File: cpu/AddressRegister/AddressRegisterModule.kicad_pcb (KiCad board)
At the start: 2 copper layers, 100 x 80 mm, 53 parts, among them J1 Bus_PCI_32bit_5V, U1 74LS193, U10 74LS245, U11 74LS245, U12 74LS00, U2 74LS193, U3 74LS193, U4 74LS193, U5 74LS245, U6 74LS245, U7 74LS245, U8 74LS245, U9 74LS245

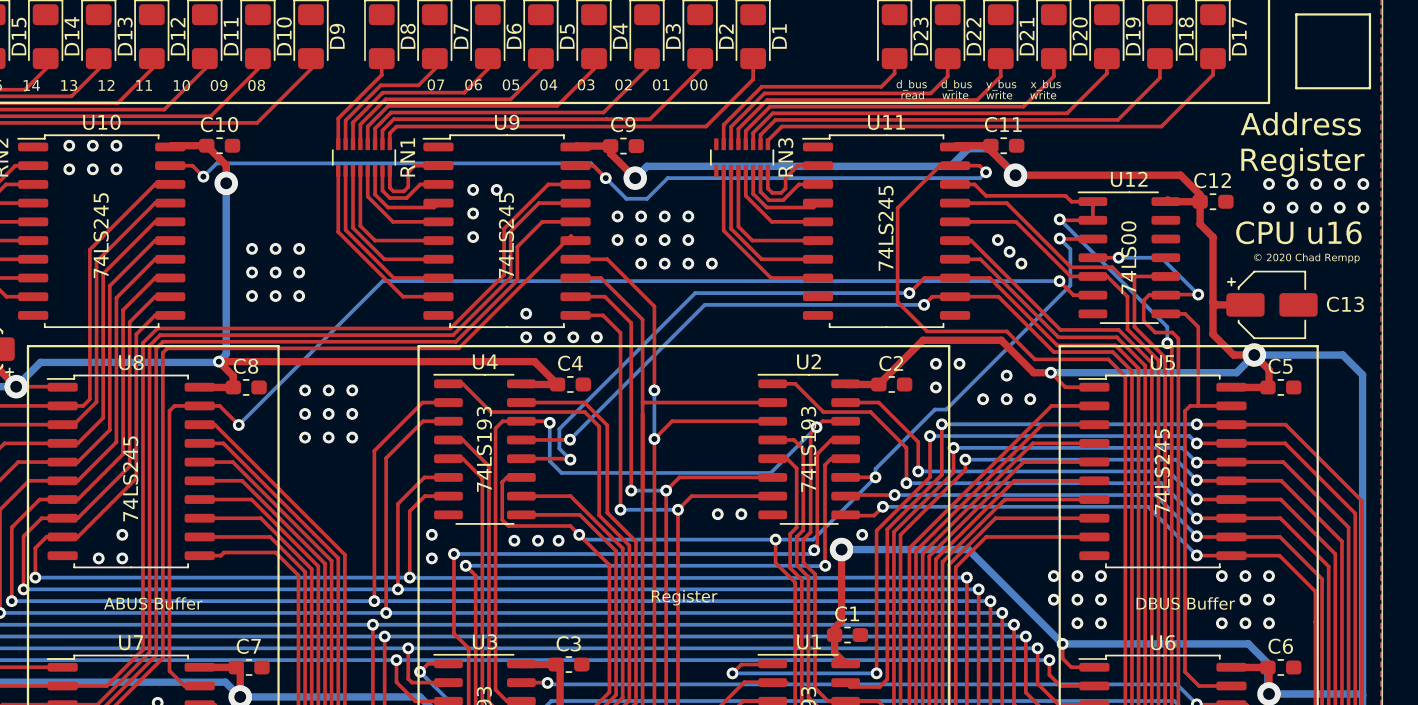
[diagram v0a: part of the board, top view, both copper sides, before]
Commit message: Finishing touches on GPR and Address Register
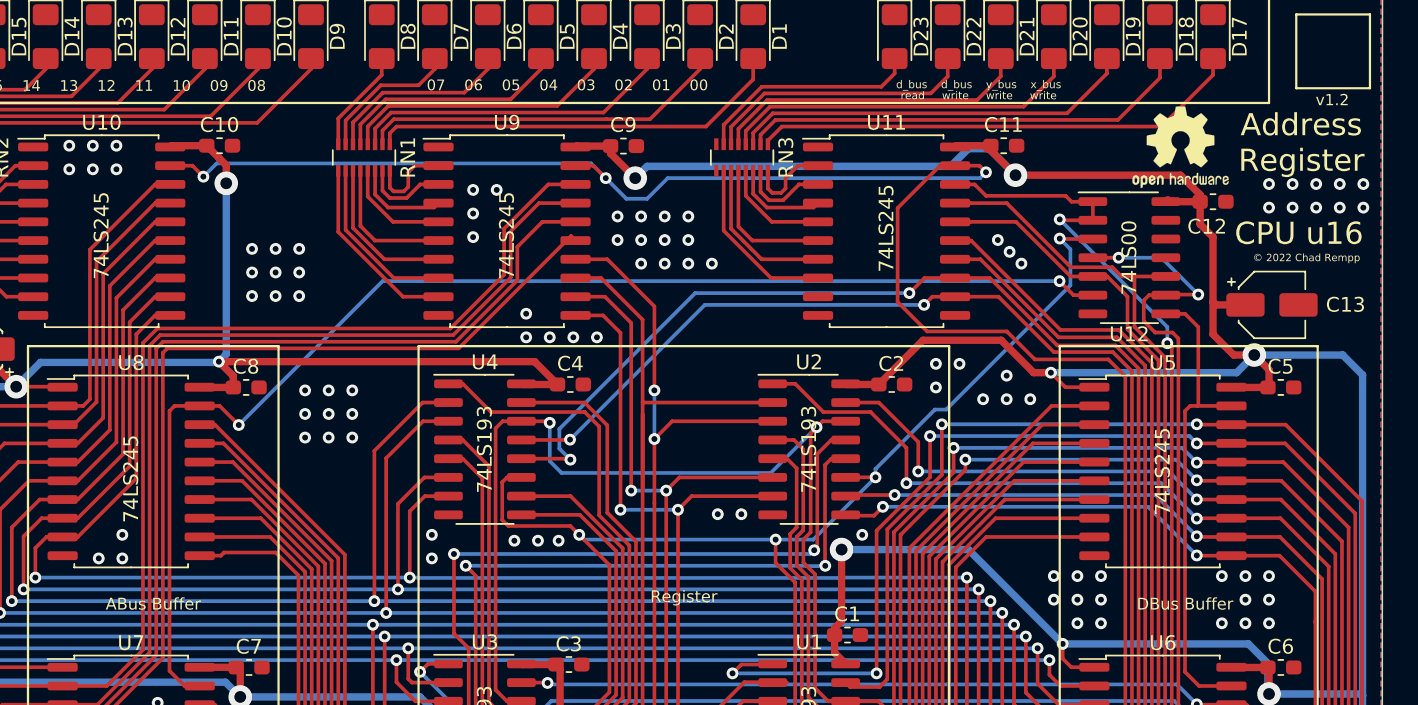
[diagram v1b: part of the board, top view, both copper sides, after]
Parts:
- added REF**: OSHW-Logo2_7.3x6mm_SilkScreen, Symbol:OSHW-Logo2_7.3x6mm_SilkScreen, F.Cu at (203.2, 51.5)
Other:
- board text added: "ABus Buffer"
- board text added: "DBus Buffer"
- board text added: "v1.2"
- board text added: "© 2022 Chad Rempp"
- board text removed: "ABUS Buffer"
- board text removed: "DBUS Buffer"
- board text removed: "© 2020 Chad Rempp"

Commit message: Upgrade to KiCad 6 and commit a bunch of random stuff
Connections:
- net /~CLK renamed /~{CLK}
- net /~DBG renamed /~{DBG}
- net /~a_bus_write_CLK renamed /~{a_bus_write_CLK}
- net /~d_bus_read renamed /~{d_bus_read}
- net /~d_bus_write_CLK renamed /~{d_bus_write_CLK}
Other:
- net class Default removed
- net class Power removed

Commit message: Address Register v1.3
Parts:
- added R1: 1K, Resistor_SMD:R_0603_1608Metric_Pad0.98x0.95mm_HandSolder, F.Cu at (150.5, 114.2)
- added R2: 1K, Resistor_SMD:R_0603_1608Metric_Pad0.98x0.95mm_HandSolder, F.Cu at (150.5, 112.6)
- added R3: 1K, Resistor_SMD:R_0603_1608Metric_Pad0.98x0.95mm_HandSolder, F.Cu at (150.5, 94.7)
- added R4: 1K, Resistor_SMD:R_0603_1608Metric_Pad0.98x0.95mm_HandSolder, F.Cu at (150.5, 96.3)
- added R5: 1K, Resistor_SMD:R_0603_1608Metric_Pad0.98x0.95mm_HandSolder, F.Cu at (128.5, 114.2)
- added R6: 1K, Resistor_SMD:R_0603_1608Metric_Pad0.98x0.95mm_HandSolder, F.Cu at (128.5, 112.6)
- added R7: 1K, Resistor_SMD:R_0603_1608Metric_Pad0.98x0.95mm_HandSolder, F.Cu at (128.5, 94.7)
- added R8: 1K, Resistor_SMD:R_0603_1608Metric_Pad0.98x0.95mm_HandSolder, F.Cu at (128.5, 96.3)
- C1, C10, C11, C12, C2, C3, C4, C5, C6, C7, C8, C9: value e -> 0.1uF
- moved D17 53.3 mm to (154.4, 59.4)
- moved D18 52.2 mm to (151.9, 59.4)
- moved D19 51.2 mm to (149.4, 59.4)
- moved D20 50.2 mm to (146.8, 59.4)
- moved D21 49.2 mm to (144.3, 59.4)
- moved D22 48.2 mm to (141.7, 59.4)
- moved D23 47.2 mm to (139.2, 59.4)
- moved D1 43.4 mm to (133.6, 59.4)
- moved C8 43.4 mm to (110.4, 99.7), turned to 0 degrees
- moved U8 42.5 mm to (106.7, 107.7)
- moved D2 42.4 mm to (131.1, 59.4)
- moved D3 41.5 mm to (128.5, 59.4)
- moved D4 40.5 mm to (126.0, 59.4)
- moved D5 39.5 mm to (123.4, 59.4)
- moved D6 38.5 mm to (120.9, 59.4)
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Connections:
- J1 pad A1: Net-(J1-PadA1) -> unconnected-(J1-PadA1)
- J1 pad A10: Net-(J1-PadA10) -> unconnected-(J1-PadA10)
- J1 pad A11: Net-(J1-PadA11) -> unconnected-(J1-PadA11)
- J1 pad A12: Net-(J1-PadA12) -> unconnected-(J1-PadA12)
- J1 pad A13: Net-(J1-PadA13) -> unconnected-(J1-PadA13)
- J1 pad A14: Net-(J1-PadA14) -> unconnected-(J1-PadA14)
- J1 pad A15: Net-(J1-PadA15) -> unconnected-(J1-PadA15)
- J1 pad A16: Net-(J1-PadA16) -> unconnected-(J1-PadA16)
- J1 pad A17: Net-(J1-PadA17) -> unconnected-(J1-PadA17)
- J1 pad A18: Net-(J1-PadA18) -> unconnected-(J1-PadA18)
- J1 pad A19: Net-(J1-PadA19) -> unconnected-(J1-PadA19)
- J1 pad A2: Net-(J1-PadA2) -> unconnected-(J1-PadA2)
- J1 pad A20: Net-(J1-PadA20) -> unconnected-(J1-PadA20)
- J1 pad A21: Net-(J1-PadA21) -> unconnected-(J1-PadA21)
- J1 pad A22: Net-(J1-PadA22) -> unconnected-(J1-PadA22)
- J1 pad A23: Net-(J1-PadA23) -> unconnected-(J1-PadA23)
- J1 pad A24: Net-(J1-PadA24) -> unconnected-(J1-PadA24)
- J1 pad A25: Net-(J1-PadA25) -> unconnected-(J1-PadA25)
- J1 pad A26: Net-(J1-PadA26) -> unconnected-(J1-PadA26)
- J1 pad A27: Net-(J1-PadA27) -> unconnected-(J1-PadA27)
- J1 pad A28: Net-(J1-PadA28) -> unconnected-(J1-PadA28)
- J1 pad A29: Net-(J1-PadA29) -> unconnected-(J1-PadA29)
- J1 pad A3: Net-(J1-PadA3) -> unconnected-(J1-PadA3)
- J1 pad A30: Net-(J1-PadA30) -> unconnected-(J1-PadA30)
- J1 pad A31: Net-(J1-PadA31) -> unconnected-(J1-PadA31)
- J1 pad A32: Net-(J1-PadA32) -> unconnected-(J1-PadA32)
- J1 pad A33: Net-(J1-PadA33) -> unconnected-(J1-PadA33)
- J1 pad A34: Net-(J1-PadA34) -> unconnected-(J1-PadA34)
- J1 pad A35: Net-(J1-PadA35) -> unconnected-(J1-PadA35)
- J1 pad A36: Net-(J1-PadA36) -> unconnected-(J1-PadA36)
- J1 pad A37: Net-(J1-PadA37) -> unconnected-(J1-PadA37)
- J1 pad A38: Net-(J1-PadA38) -> unconnected-(J1-PadA38)
- J1 pad A39: Net-(J1-PadA39) -> unconnected-(J1-PadA39)
- J1 pad A4: Net-(J1-PadA4) -> unconnected-(J1-PadA4)
- J1 pad A40: Net-(J1-PadA40) -> unconnected-(J1-PadA40)
- J1 pad A41: Net-(J1-PadA41) -> unconnected-(J1-PadA41)
- J1 pad A42: Net-(J1-PadA42) -> unconnected-(J1-PadA42)
- J1 pad A43: Net-(J1-PadA43) -> unconnected-(J1-PadA43)
- J1 pad A44: Net-(J1-PadA44) -> unconnected-(J1-PadA44)
- J1 pad A45: Net-(J1-PadA45) -> unconnected-(J1-PadA45)
- J1 pad A46: Net-(J1-PadA46) -> unconnected-(J1-PadA46)
- J1 pad A47: Net-(J1-PadA47) -> unconnected-(J1-PadA47)
- J1 pad A48: Net-(J1-PadA48) -> unconnected-(J1-PadA48)
- J1 pad A49: Net-(J1-PadA49) -> unconnected-(J1-PadA49)
- J1 pad A5: Net-(J1-PadA5) -> unconnected-(J1-PadA5)
- J1 pad A6: Net-(J1-PadA6) -> unconnected-(J1-PadA6)
- J1 pad A7: Net-(J1-PadA7) -> unconnected-(J1-PadA7)
- J1 pad A8: Net-(J1-PadA8) -> unconnected-(J1-PadA8)
- J1 pad A9: Net-(J1-PadA9) -> unconnected-(J1-PadA9)
- J1 pad B1: Net-(J1-PadB1) -> unconnected-(J1-PadB1)
- J1 pad B10: Net-(J1-PadB10) -> unconnected-(J1-PadB10)
- J1 pad B11: Net-(J1-PadB11) -> unconnected-(J1-PadB11)
- J1 pad B12: Net-(J1-PadB12) -> unconnected-(J1-PadB12)
- J1 pad B13: Net-(J1-PadB13) -> unconnected-(J1-PadB13)
- J1 pad B14: Net-(J1-PadB14) -> unconnected-(J1-PadB14)
- J1 pad B15: Net-(J1-PadB15) -> unconnected-(J1-PadB15)
- J1 pad B16: Net-(J1-PadB16) -> unconnected-(J1-PadB16)
- J1 pad B17: Net-(J1-PadB17) -> unconnected-(J1-PadB17)
- J1 pad B2: Net-(J1-PadB2) -> unconnected-(J1-PadB2)
- J1 pad B3: Net-(J1-PadB3) -> unconnected-(J1-PadB3)
- J1 pad B4: Net-(J1-PadB4) -> unconnected-(J1-PadB4)
- J1 pad B5: Net-(J1-PadB5) -> unconnected-(J1-PadB5)
- J1 pad B54: Net-(J1-PadB54) -> unconnected-(J1-PadB54)
- J1 pad B55: Net-(J1-PadB55) -> unconnected-(J1-PadB55)
- J1 pad B58: /HLT -> unconnected-(J1-PadB58)
- J1 pad B59: /~{CLK} -> unconnected-(J1-PadB59)
- J1 pad B6: Net-(J1-PadB6) -> unconnected-(J1-PadB6)
- J1 pad B7: Net-(J1-PadB7) -> unconnected-(J1-PadB7)
- J1 pad B8: Net-(J1-PadB8) -> unconnected-(J1-PadB8)
- J1 pad B9: Net-(J1-PadB9) -> unconnected-(J1-PadB9)
- RN3 pad 8: Net-(RN3-Pad8) -> unconnected-(RN3-Pad8)
- RN3 pad 9: Net-(RN3-Pad9) -> unconnected-(RN3-Pad9)
- U11 pad 11: Net-(U11-Pad11) -> unconnected-(U11-Pad11)
- U11 pad 9: Net-(U11-Pad9) -> unconnected-(U11-Pad9)
- U12 pad 11: Net-(U12-Pad11) -> unconnected-(U12-Pad11)
- U12 pad 12: Net-(U12-Pad12) -> unconnected-(U12-Pad12)
- U12 pad 13: Net-(U12-Pad13) -> unconnected-(U12-Pad13)
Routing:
- net +5V: track 540.7 -> 455.0 mm, vias 15 -> 14
- net /reg_01: track 202.9 -> 135.7 mm, vias 3 -> 5
- net /reg_04: track 159.4 -> 92.3 mm, vias 5 -> 4
- net /reg_00: track 205.8 -> 139.3 mm, vias 3 -> 5
- net /reg_05: track 157.7 -> 95.3 mm, vias 3 -> 4
- net /reg_06: track 146.7 -> 90.9 mm, vias 5 -> 4
- net /reg_02: track 190.1 -> 139.5 mm, vias 3 -> 5
- net /reg_07: track 140.6 -> 90.7 mm, vias 5 -> 4
- net /d_bus_04: track 102.5 -> 149.6 mm, vias 2 -> 4
- net /reg_03: track 182.2 -> 138.2 mm, vias 3 -> 5
- net /d_bus_06: track 97.5 -> 140.4 mm, vias 2 -> 4
- net /d_bus_07: track 100.3 -> 137.3 mm, vias 2 -> 4
- net /d_bus_05: track 107.6 -> 141.4 mm, vias 2 -> 4
- net /d_bus_15: track 123.8 -> 96.1 mm
- net /a_bus_15: track 51.0 -> 24.7 mm
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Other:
- board text added: "0"
- board text added: "1"
- board text added: "10"
- board text added: "11"
- board text added: "12"
- board text added: "13"
- board text added: "14"
- board text added: "15"
- board text added: "2"
- board text added: "3"
- board text added: "4"
- board text added: "5"
- board text added: "6"
- board text added: "7"
- board text added: "8"
- board text added: "9"
- board text added: "a_bus write"
- board text added: "borrow"
- board text added: "carry"
- board text added: "d_bus read"
- board text added: "d_bus write"
- board text added: "dec"
- board text added: "inc"
- board text removed: "07 06 05 04 03 02 01 00"
- board text removed: "15 14 13 12 11 10 09 08"
- board text removed: "d_bus d_bus y_bus x_bus"
- board text removed: "read write write write"
